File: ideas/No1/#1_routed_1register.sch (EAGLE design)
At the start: 17 parts, among them IC1 ULN2803, IC2 ULN2803, IC3 TD620831A, IC4 TD620831A, U1 SN74HC595N, U2 SN74HC595N, U3 SN74HC595N, U4 SN74HC595N

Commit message: 1_route_1register.sch
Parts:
- removed C5: 10nF, resistor:C-EU025-025X050
- removed IC1: ULN2803, uln-udn:ULN2803A
- removed IC3, IC4: TD620831A, td62083-dil:TD620831A
- removed L, R: C-GRID-16-70543, con-molex:C-GRID-16-70543
- removed U4: SN74HC595N, SparkFun-IC-Logic:74HC595N
- added C1-C8: ULN2803, uln-udn:ULN2803A
- added D1: 1N4004, diode:1N4004
- added P1-O8RIGHT, P1-P8LEFT: TD620831A, td62083-dil:TD620831A
- added SV1: (no value), con-lstb:MA03-1
- added SV2, SV3, SV4, SV5: (no value), con-lsta:FE08-1
- added U$2: DC-DC-STEP-DOWN-LM2596, diy-modules_lm2596:DC-DC-STEP-DOWN-LM2596
- renumbered IC2 to B1-B8
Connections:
- removed net N$10: IC3.O2, L-2.S
- removed net N$11: IC3.O3, L-3.S
- removed net N$12: IC3.O4, L-4.S
- removed net N$13: IC3.O5, L-5.S
- removed net N$14: IC3.O6, L-6.S
- removed net N$15: IC3.O7, L-7.S
- removed net N$16: IC3.O8, L-8.S
- removed net N$17: B1-B8.O8, L-16.S
- removed net N$18: B1-B8.O7, L-15.S
- removed net N$19: B1-B8.O6, L-14.S
- removed net N$20: B1-B8.O5, L-13.S
- removed net N$21: B1-B8.O4, L-12.S
- removed net N$22: B1-B8.O3, L-11.S
- removed net N$23: B1-B8.O2, L-10.S
- removed net N$24: B1-B8.O1, L-9.S
- removed net N$26: IC4.O2, R-2.S
- removed net N$28: IC4.O4, R-4.S
- removed net N$30: IC4.O6, R-6.S
- removed net N$33: IC4.O8, R-8.S
- removed net N$35: IC4.I8, U3.QH
- removed net N$39: IC1.O8, R-16.S
- removed net N$40: IC1.O7, R-15.S
- removed net N$49: IC1.O6, R-14.S
- removed net N$50: IC1.O5, R-13.S
- removed net N$51: IC1.O4, R-12.S
- removed net N$52: IC1.O3, R-11.S
- removed net N$53: IC1.O2, R-10.S
- removed net N$54: IC1.O1, R-9.S
- removed net N$57: IC4.O1, R-1.S
- removed net N$59: IC4.O3, R-3.S
- removed net N$61: IC4.O5, R-5.S
- removed net N$63: IC4.O7, R-7.S
- removed net N$73: IC4.I2, U3.QB
- removed net N$74: IC4.I3, U3.QC
- removed net N$75: IC4.I4, U3.QD
- removed net N$76: IC4.I5, U3.QE
- removed net N$77: U2.QH*, U4.SER
- removed net N$78: IC4.I7, U3.QG
- removed net N$83: IC1.I1, U4.QA
- removed net N$84: IC1.I2, U4.QB
- removed net N$85: IC1.I3, U4.QC
- removed net N$86: IC1.I4, U4.QD
- removed net N$87: IC1.I5, U4.QE
- removed net N$88: IC1.I6, U4.QF
- removed net N$89: IC1.I7, U4.QG
- removed net N$9: IC3.O1, L-1.S
- removed net N$90: IC1.I8, U4.QH
- new net 24V: P1-O8RIGHT.VS, P1-P8LEFT.VS, SV1.1, U$2.IN+
- new net GND: B1-B8.GND, C1-C8.GND, C1.1, C2.-, C3.1, C4.1, C6.2, P1-O8RIGHT.GND, P1-P8LEFT.GND, U$1.GND, U1.GND, U2.GND, U3.GND
- new net N$25: P1-P8LEFT.I1, U1.QH
- new net N$27: P1-P8LEFT.I2, U1.QG
- new net N$29: P1-P8LEFT.I3, U1.QF
- new net N$32: P1-P8LEFT.I5, U1.QD
- new net N$55: P1-O8RIGHT.I7, U3.QB
- new net N$56: P1-O8RIGHT.I8, U3.QA
- new net N$69: D1.A, U$2.OUT+
- net 3.3V: now also SV1.3, U$2.IN-, U$2.OUT-; no longer B1-B8.GND, C1.1, C2.-, C3.1, C4.1, C5.1, C6.2, IC1.GND, IC3.GND, IC4.GND, U$1.GND, U1.GND, U2.GND, U3.GND, U4.GND
- net N$1: now also U2.QH; no longer U2.QA
- net N$2: now also U2.QG; no longer U2.QB
- net N$3: now also U2.QF; no longer U2.QC
- net N$31: now also P1-P8LEFT.I4, U1.QE; no longer IC3.I8, U1.QH
- net N$38: no longer U4.RCK
- net N$4: now also U2.QE; no longer U2.QD
- net N$41: now also P1-P8LEFT.I6, U1.QC; no longer IC3.I1, U1.QA
- net N$42: now also P1-P8LEFT.I7; no longer IC3.I2
- net N$43: now also P1-P8LEFT.I8, U1.QA; no longer IC3.I3, U1.QC
- net N$44: now also P1-O8RIGHT.I2, U3.QG; no longer IC3.I4, U1.QD
- net N$45: now also P1-O8RIGHT.I3, U3.QF; no longer IC3.I5, U1.QE
- net N$46: now also P1-O8RIGHT.I4, U3.QE; no longer IC4.I6, U3.QF
- net N$47: now also P1-O8RIGHT.I5, U3.QD; no longer IC3.I7, U1.QG
- net N$48: now also P1-O8RIGHT.I6, U3.QC; no longer IC3.I6, U1.QF
- net N$5: now also U2.QD; no longer U2.QE
- net N$6: now also U2.QC; no longer U2.QF
- net N$7: now also U2.QB; no longer U2.QG
- net N$72: now also P1-O8RIGHT.I1, U3.QH; no longer IC4.I1, U3.QA
- net N$8: now also U2.QA; no longer U2.QH
- net N$80: no longer U4.SCK
- net VCC: now also D1.C; no longer C5.2, IC3.VS, IC4.VS, U4.VCC
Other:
- moved on the sheet: C1, C2, C4, C6, U1, U3

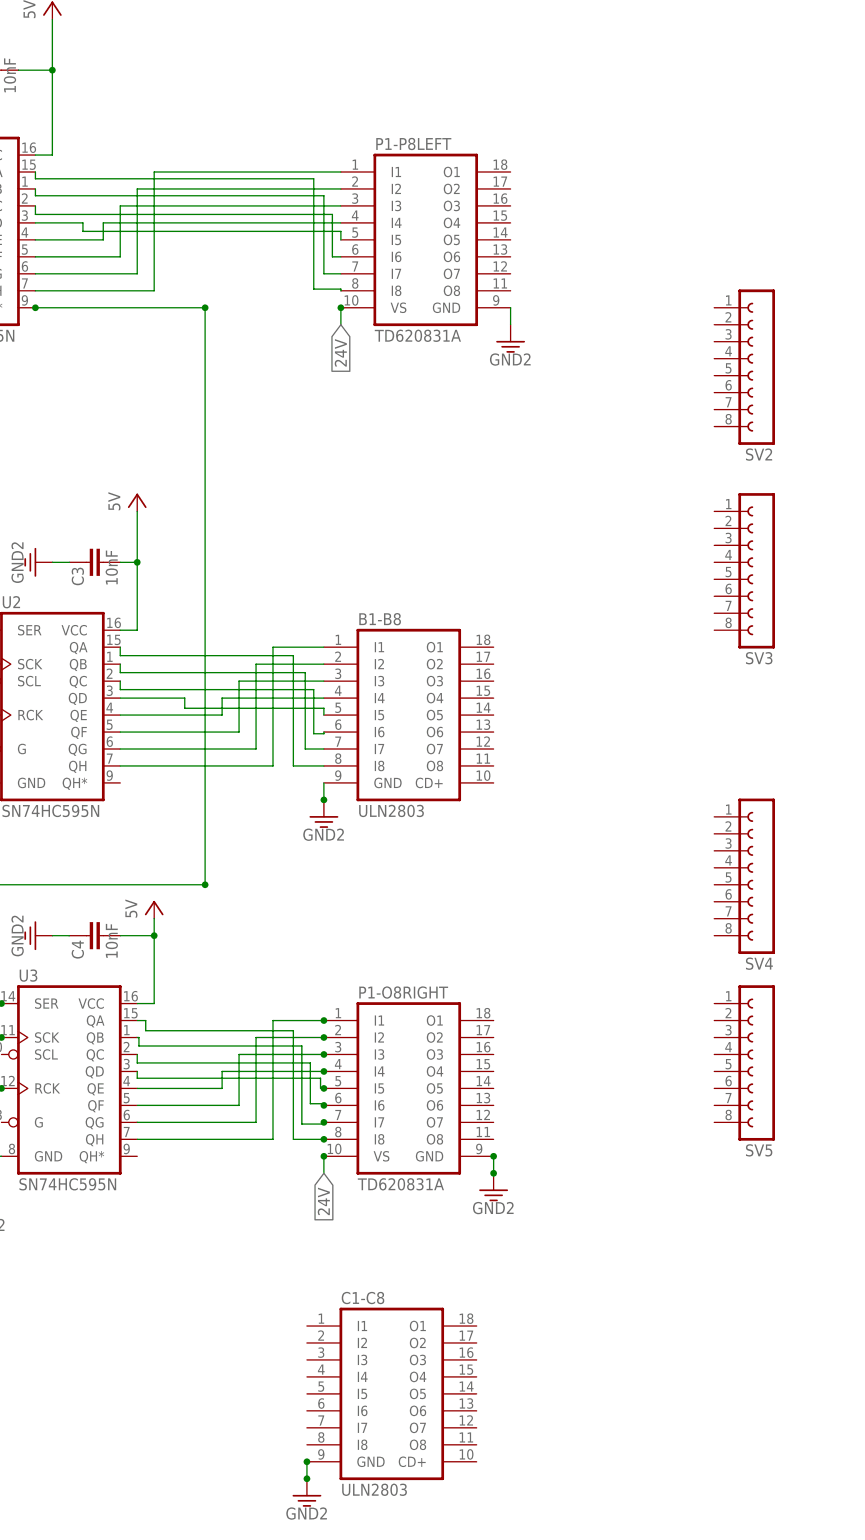
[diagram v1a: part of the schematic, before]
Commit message: update picture with cable pins
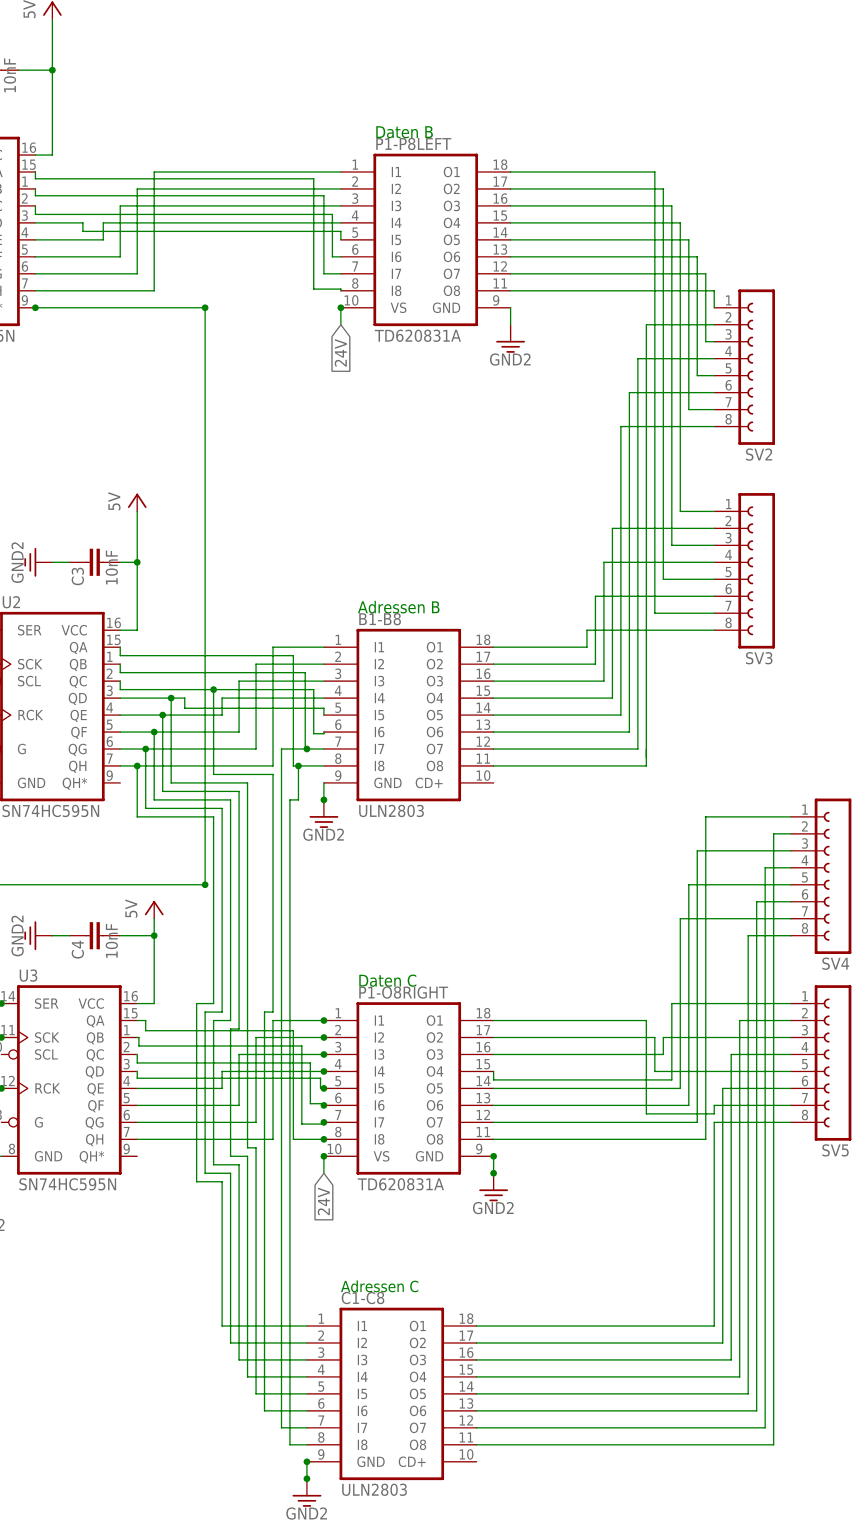
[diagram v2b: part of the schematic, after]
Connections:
- new net N$10: P1-P8LEFT.O7, SV2.3
- new net N$11: P1-P8LEFT.O6, SV2.5
- new net N$12: B1-B8.O4, SV3.2
- new net N$13: P1-P8LEFT.O5, SV2.7
- new net N$14: P1-P8LEFT.O4, SV3.1
- new net N$15: P1-P8LEFT.O3, SV3.3
- new net N$16: P1-P8LEFT.O2, SV3.5
- new net N$17: P1-P8LEFT.O1, SV3.7
- new net N$18: B1-B8.O8, SV2.2
- new net N$19: B1-B8.O7, SV2.4
- new net N$21: B1-B8.O6, SV2.6
- new net N$22: B1-B8.O5, SV2.8
- new net N$23: B1-B8.O3, SV3.4
- new net N$24: B1-B8.O2, SV3.6
- new net N$26: B1-B8.O1, SV3.8
- new net N$28: P1-O8RIGHT.O7, SV4.3
- new net N$30: P1-O8RIGHT.O8, SV4.1
- new net N$33: C1-C8.O2, SV5.6
- new net N$35: P1-O8RIGHT.O5, SV4.7
- new net N$39: P1-O8RIGHT.O4, SV5.1
- new net N$40: P1-O8RIGHT.O3, SV5.3
- new net N$49: P1-O8RIGHT.O6, SV4.5
- new net N$50: P1-O8RIGHT.O2, SV5.5
- new net N$51: P1-O8RIGHT.O1, SV5.7
- new net N$52: C1-C8.O1, SV5.8
- new net N$53: C1-C8.O3, SV5.4
- new net N$54: C1-C8.O4, SV5.2
- new net N$57: C1-C8.O5, SV4.8
- new net N$58: C1-C8.O6, SV4.6
- new net N$59: C1-C8.O7, SV4.4
- new net N$60: C1-C8.O8, SV4.2
- new net N$9: P1-P8LEFT.O8, SV2.1
- net N$1: now also B1-B8.I7, C1-C8.I7, U2.QB; no longer B1-B8.I1, U2.QH
- net N$2: now also C1-C8.I2
- net N$3: now also C1-C8.I3
- net N$4: now also C1-C8.I4
- net N$5: now also C1-C8.I5
- net N$6: now also C1-C8.I6
- net N$7: now also B1-B8.I1, C1-C8.I1, U2.QH; no longer B1-B8.I7, U2.QB
- net N$8: now also C1-C8.I8
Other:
- note added: "Adressen B"
- note added: "Adressen C"
- note added: "Daten B"
- note added: "Daten C"
- moved on the sheet: SV4, SV5

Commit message: update picture with cable pins
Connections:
- removed net 3.3V: SV1.3, U$2.IN-, U$2.OUT-
- new net N$61: SV1.3, U$2.IN-
- net GND: now also U$2.OUT-
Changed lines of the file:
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@@
 <part name="P1-P8LEFT" library="td62083-dil" deviceset="TD62083" device="A" package3d_urn="urn:adsk.eagle:package:16424/2" technology="1"/>
 <part name="U$2" library="diy-modules_lm2596" deviceset="DC-DC-STEP-DOWN-LM2596" device=""/>
-<part name="GND14" library="SparkFun-PowerSymbols" library_urn="urn:adsk.eagle:library:530" deviceset="GND2" device=""/>
-<part name="GND15" library="SparkFun-PowerSymbols" library_urn="urn:adsk.eagle:library:530" deviceset="GND2" device=""/>
 <part name="D1" library="diode" library_urn="urn:adsk.eagle:library:210" deviceset="1N4004" device="" package3d_urn="urn:adsk.eagle:package:43336/1"/>
 <part name="5V5" library="supply1" library_urn="urn:adsk.eagle:library:371" deviceset="VCC" device="" value="5V"/>
@@
 <attribute name="VALUE" x="-200.66" y="53.34" size="1.778" layer="96" rot="R180"/>
 </instance>
-<instance part="GND14" gate="G$1" x="-238.76" y="71.12" smashed="yes" rot="R270">
-<attribute name="VALUE" x="-240.538" y="71.12" size="1.778" layer="96" rot="R270" align="top-center"/>
-</instance>
-<instance part="GND15" gate="G$1" x="-185.42" y="73.66" smashed="yes" rot="R180">
-<attribute name="VALUE" x="-185.42" y="75.438" size="1.778" layer="96" rot="R180" align="top-center"/>
-</instance>
 <instance part="D1" gate="1" x="-238.76" y="-2.54" smashed="yes" rot="MR180">
 <attribute name="NAME" x="-236.22" y="-3.0226" size="1.778" layer="95" rot="MR180"/>
@@
 <pinref part="GND2" gate="G$1" pin="3.3V"/>
 <pinref part="C3" gate="G$1" pin="1"/>
-<wire x1="-88.9" y1="40.64" x2="-86.36" y2="40.64" width="0.1524" layer="91"/>
+<wire x1="-88.9" y1="40.64" x2="-87.63" y2="40.64" width="0.1524" layer="91"/>
+<wire x1="-87.63" y1="40.64" x2="-86.36" y2="40.64" width="0.1524" layer="91"/>
+<wire x1="-87.63" y1="40.64" x2="-87.63" y2="55.88" width="0.1524" layer="91"/>
+<junction x="-87.63" y="40.64"/>
+<wire x1="-87.63" y1="55.88" x2="-148.59" y2="55.88" width="0.1524" layer="91"/>
+<wire x1="-148.59" y1="55.88" x2="-148.59" y2="86.36" width="0.1524" layer="91"/>
+<wire x1="-148.59" y1="86.36" x2="-234.95" y2="86.36" width="0.1524" layer="91"/>
+<pinref part="U$2" gate="G$1" pin="OUT-"/>
+<wire x1="-231.14" y1="71.12" x2="-234.95" y2="71.12" width="0.1524" layer="91"/>
+<wire x1="-234.95" y1="86.36" x2="-234.95" y2="71.12" width="0.1524" layer="91"/>
 </segment>
 <segment>
@@
 </segment>
 </net>
-<net name="3.3V" class="0">
-<segment>
-<pinref part="U$2" gate="G$1" pin="OUT-"/>
-<wire x1="-231.14" y1="71.12" x2="-236.22" y2="71.12" width="0.1524" layer="91"/>
-<pinref part="GND14" gate="G$1" pin="3.3V"/>
-</segment>
-<segment>
-<pinref part="U$2" gate="G$1" pin="IN-"/>
-<wire x1="-195.58" y1="71.12" x2="-185.42" y2="71.12" width="0.1524" layer="91"/>
-<pinref part="GND15" gate="G$1" pin="3.3V"/>
-<pinref part="SV1" gate="G$1" pin="3"/>
-<wire x1="-162.56" y1="73.66" x2="-162.56" y2="71.12" width="0.1524" layer="91"/>
-<wire x1="-185.42" y1="71.12" x2="-162.56" y2="71.12" width="0.1524" layer="91"/>
-<junction x="-185.42" y="71.12"/>
-<junction x="-162.56" y="73.66"/>
-<junction x="-162.56" y="71.12"/>
-<junction x="-195.58" y="71.12"/>
-</segment>
-</net>
 <net name="N$69" class="0">
 <segment>
@@
 </segment>
 </net>
+<net name="N$61" class="0">
+<segment>
+<pinref part="U$2" gate="G$1" pin="IN-"/>
+<pinref part="SV1" gate="G$1" pin="3"/>
+<wire x1="-162.56" y1="73.66" x2="-162.56" y2="71.12" width="0.1524" layer="91"/>
+<wire x1="-195.58" y1="71.12" x2="-162.56" y2="71.12" width="0.1524" layer="91"/>
+<junction x="-162.56" y="73.66"/>
+<junction x="-162.56" y="71.12"/>
+<junction x="-195.58" y="71.12"/>
+</segment>
+</net>

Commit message: 1_route_1register.sch updated
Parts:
- removed SV2, SV3, SV4, SV5: (no value), con-lsta:FE08-1
- added HEADB1-B8, HEADC1-C8, HEADP1-8LEFT, HEADP1-P8RIGHT: (no value), con-lsta:FE08-1
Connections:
- removed net N$60: C1-C8.O8, SV4.2
- new net N$20: HEADP1-8LEFT.1, P1-P8LEFT.O1
- net N$10: now also HEADP1-8LEFT.3, P1-P8LEFT.O3; no longer P1-P8LEFT.O7, SV2.3
- net N$11: now also HEADP1-8LEFT.4, P1-P8LEFT.O4; no longer P1-P8LEFT.O6, SV2.5
- net N$12: now also HEADP1-8LEFT.5, P1-P8LEFT.O5; no longer B1-B8.O4, SV3.2
- net N$13: now also HEADP1-8LEFT.6, P1-P8LEFT.O6; no longer P1-P8LEFT.O5, SV2.7
- net N$14: now also HEADP1-8LEFT.7, P1-P8LEFT.O7; no longer P1-P8LEFT.O4, SV3.1
- net N$15: now also HEADP1-8LEFT.8, P1-P8LEFT.O8; no longer P1-P8LEFT.O3, SV3.3
- net N$16: now also B1-B8.O1, HEADB1-B8.1; no longer P1-P8LEFT.O2, SV3.5
- net N$17: now also B1-B8.O2, HEADB1-B8.2; no longer P1-P8LEFT.O1, SV3.7
- net N$18: now also B1-B8.O3, HEADB1-B8.3; no longer B1-B8.O8, SV2.2
- net N$19: now also B1-B8.O4, HEADB1-B8.4; no longer B1-B8.O7, SV2.4
- net N$21: now also B1-B8.O5, HEADB1-B8.5; no longer B1-B8.O6, SV2.6
- net N$22: now also B1-B8.O6, HEADB1-B8.6; no longer B1-B8.O5, SV2.8
- net N$23: now also B1-B8.O7, HEADB1-B8.7; no longer B1-B8.O3, SV3.4
- net N$24: now also B1-B8.O8, HEADB1-B8.8; no longer B1-B8.O2, SV3.6
- net N$26: now also HEADP1-P8RIGHT.1, P1-O8RIGHT.O1; no longer B1-B8.O1, SV3.8
- net N$28: now also HEADP1-P8RIGHT.3, P1-O8RIGHT.O3; no longer P1-O8RIGHT.O7, SV4.3
- net N$30: now also HEADP1-P8RIGHT.2, P1-O8RIGHT.O2; no longer P1-O8RIGHT.O8, SV4.1
- net N$33: now also HEADP1-P8RIGHT.5, P1-O8RIGHT.O5; no longer C1-C8.O2, SV5.6
- net N$35: now also HEADP1-P8RIGHT.6, P1-O8RIGHT.O6; no longer P1-O8RIGHT.O5, SV4.7
- net N$39: now also HEADP1-P8RIGHT.4; no longer SV5.1
- net N$40: now also HEADP1-P8RIGHT.7, P1-O8RIGHT.O7; no longer P1-O8RIGHT.O3, SV5.3
- net N$49: now also HEADP1-P8RIGHT.8, P1-O8RIGHT.O8; no longer P1-O8RIGHT.O6, SV4.5
- net N$50: now also C1-C8.O1, HEADC1-C8.1; no longer P1-O8RIGHT.O2, SV5.5
- net N$51: now also C1-C8.O2, HEADC1-C8.2; no longer P1-O8RIGHT.O1, SV5.7
- net N$52: now also C1-C8.O3, HEADC1-C8.3; no longer C1-C8.O1, SV5.8
- net N$53: now also C1-C8.O4, HEADC1-C8.4; no longer C1-C8.O3, SV5.4
- net N$54: now also C1-C8.O5, HEADC1-C8.5; no longer C1-C8.O4, SV5.2
- net N$57: now also C1-C8.O6, HEADC1-C8.6; no longer C1-C8.O5, SV4.8
- net N$58: now also C1-C8.O7, HEADC1-C8.7; no longer C1-C8.O6, SV4.6
- net N$59: now also C1-C8.O8, HEADC1-C8.8; no longer C1-C8.O7, SV4.4
- net N$9: now also HEADP1-8LEFT.2, P1-P8LEFT.O2; no longer P1-P8LEFT.O8, SV2.1

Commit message: 1_route_1register.sch updated
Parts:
- removed D1: 1N4004, diode:1N4004
- added 1N4007: (no value), resistor:R-EU_0207/15
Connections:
- removed net N$79: U$1.D0, U1.SCK, U3.SCK
- new net N$60: U$1.D3, U1.SCK, U3.SCK
- net N$34: now also U$1.D1; no longer U$1.D6
- net N$36: now also U$1.D2; no longer U$1.D5
- net N$37: now also U$1.D6; no longer U$1.D3
- net N$38: now also U$1.D0; no longer U$1.D1
- net N$69: now also 1N4007.1; no longer D1.A
- net N$80: now also U$1.D5; no longer U$1.D2
- net VCC: now also 1N4007.2; no longer D1.C
